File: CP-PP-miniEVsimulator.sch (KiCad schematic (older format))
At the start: 25 parts, among them J1 Conn_01x01_Female, J2 Conn_01x01_Female, J3 Conn_01x01_Female

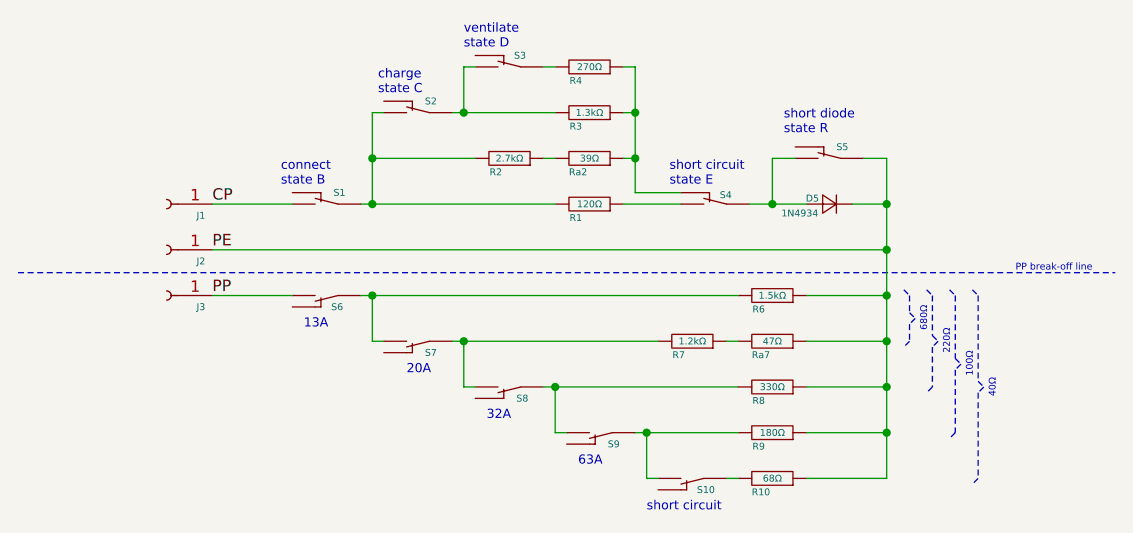
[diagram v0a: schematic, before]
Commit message: cutouts mirrored
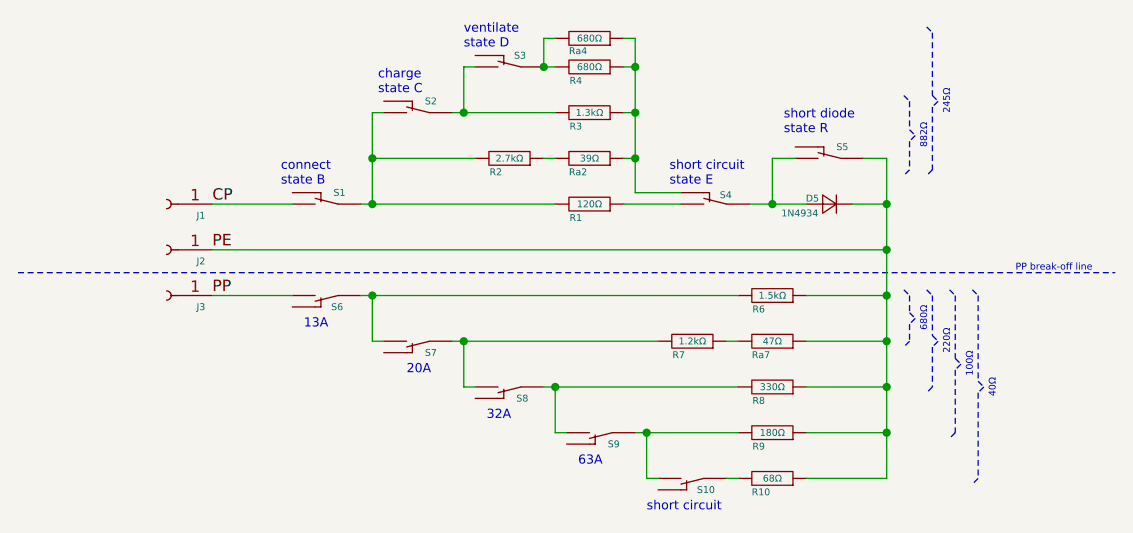
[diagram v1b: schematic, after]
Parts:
- added Ra4: 680Ω, Resistor_THT:R_Axial_DIN0207_L6.3mm_D2.5mm_P7.62mm_Horizontal, symbol _sauttefk:R
- D5: LCSC (none) -> C146704
- R1: LCSC (none) -> C58619
- R10: LCSC (none) -> C58629
- R2: LCSC (none) -> C58615
- R3: LCSC (none) -> C337167
- R4: value 270Ω -> 680Ω; LCSC (none) -> C58599
- R6: LCSC (none) -> C58620
- R7: LCSC (none) -> C58590
- R8: LCSC (none) -> C58608
- R9: LCSC (none) -> C58665
- Ra2: LCSC (none) -> C58644
- Ra7: LCSC (none) -> C58604
- S1, S10, S2, S3, S4, S5, S6, S7, S8, S9: LCSC (none) -> C312276
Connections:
- net at R3.1, R4.1, Ra2.1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: now also Ra4.1
- net at R4.2, S3.1 (COM): now also Ra4.2
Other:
- note added: "245Ω"
- note added: "882Ω"
